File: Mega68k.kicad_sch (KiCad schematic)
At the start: 15 parts, among them J1 CLK Select, J2 Ext CLK, J3 SPI, U1 68000D, U2 AS6C4008-55PCN, U3 AS6C4008-55PCN, X1 CXO_DIP8

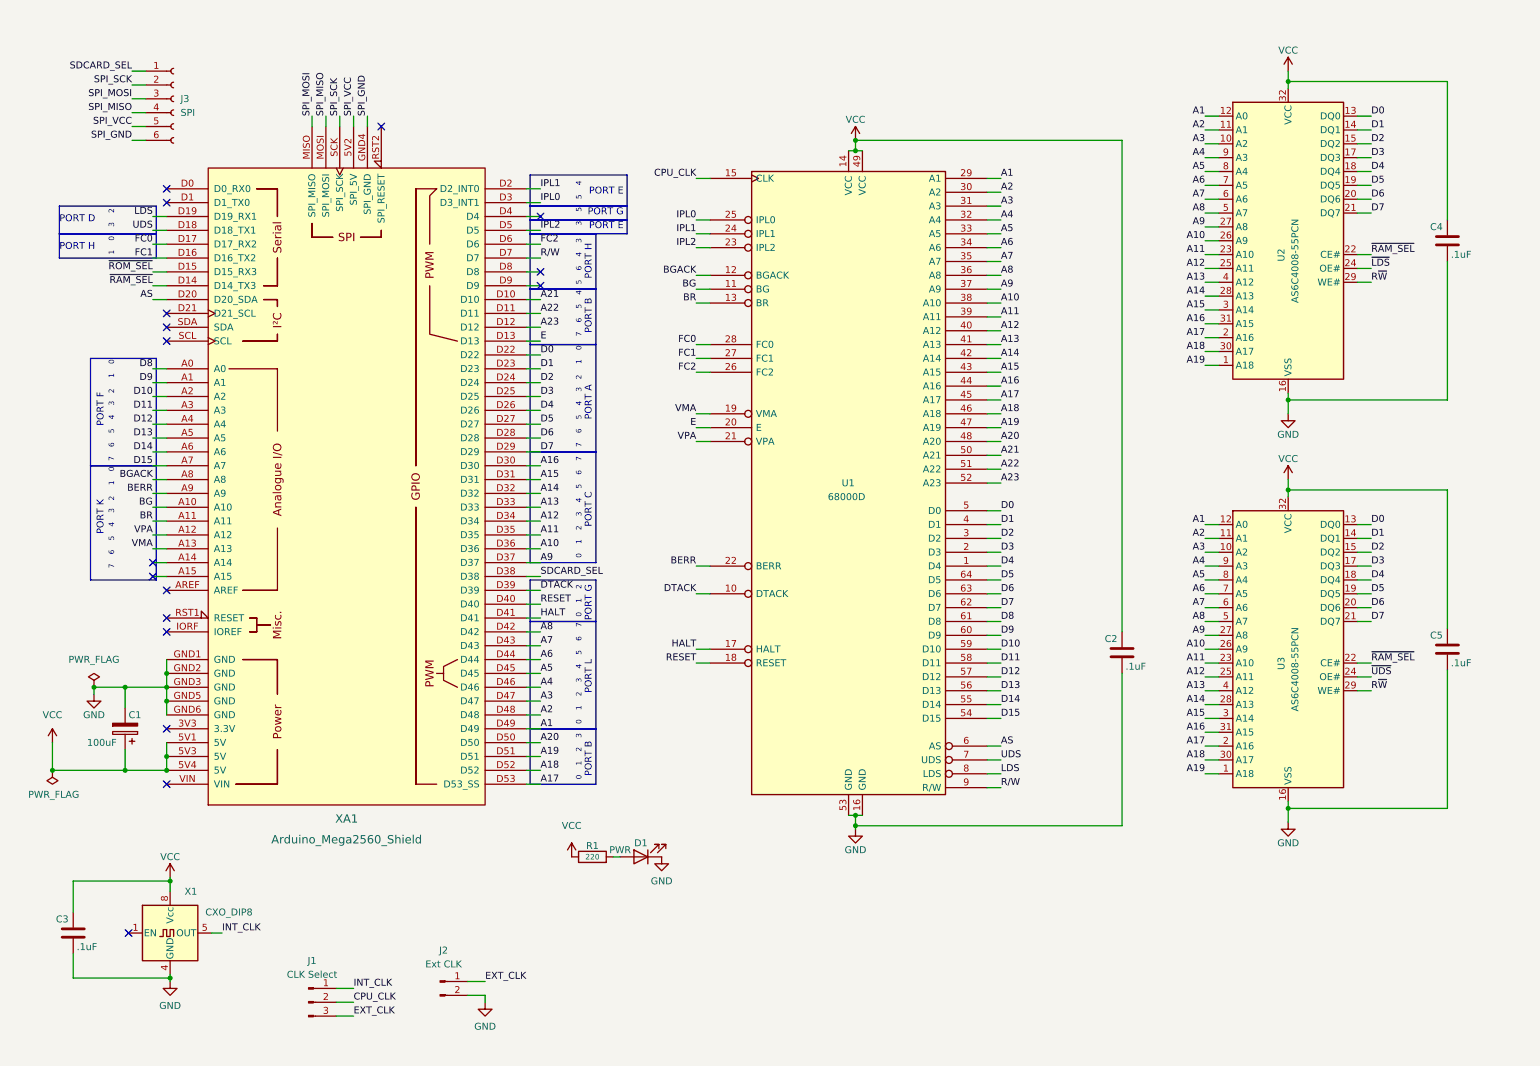
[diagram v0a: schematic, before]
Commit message: Fixed 64 pin socket size and added more status lights
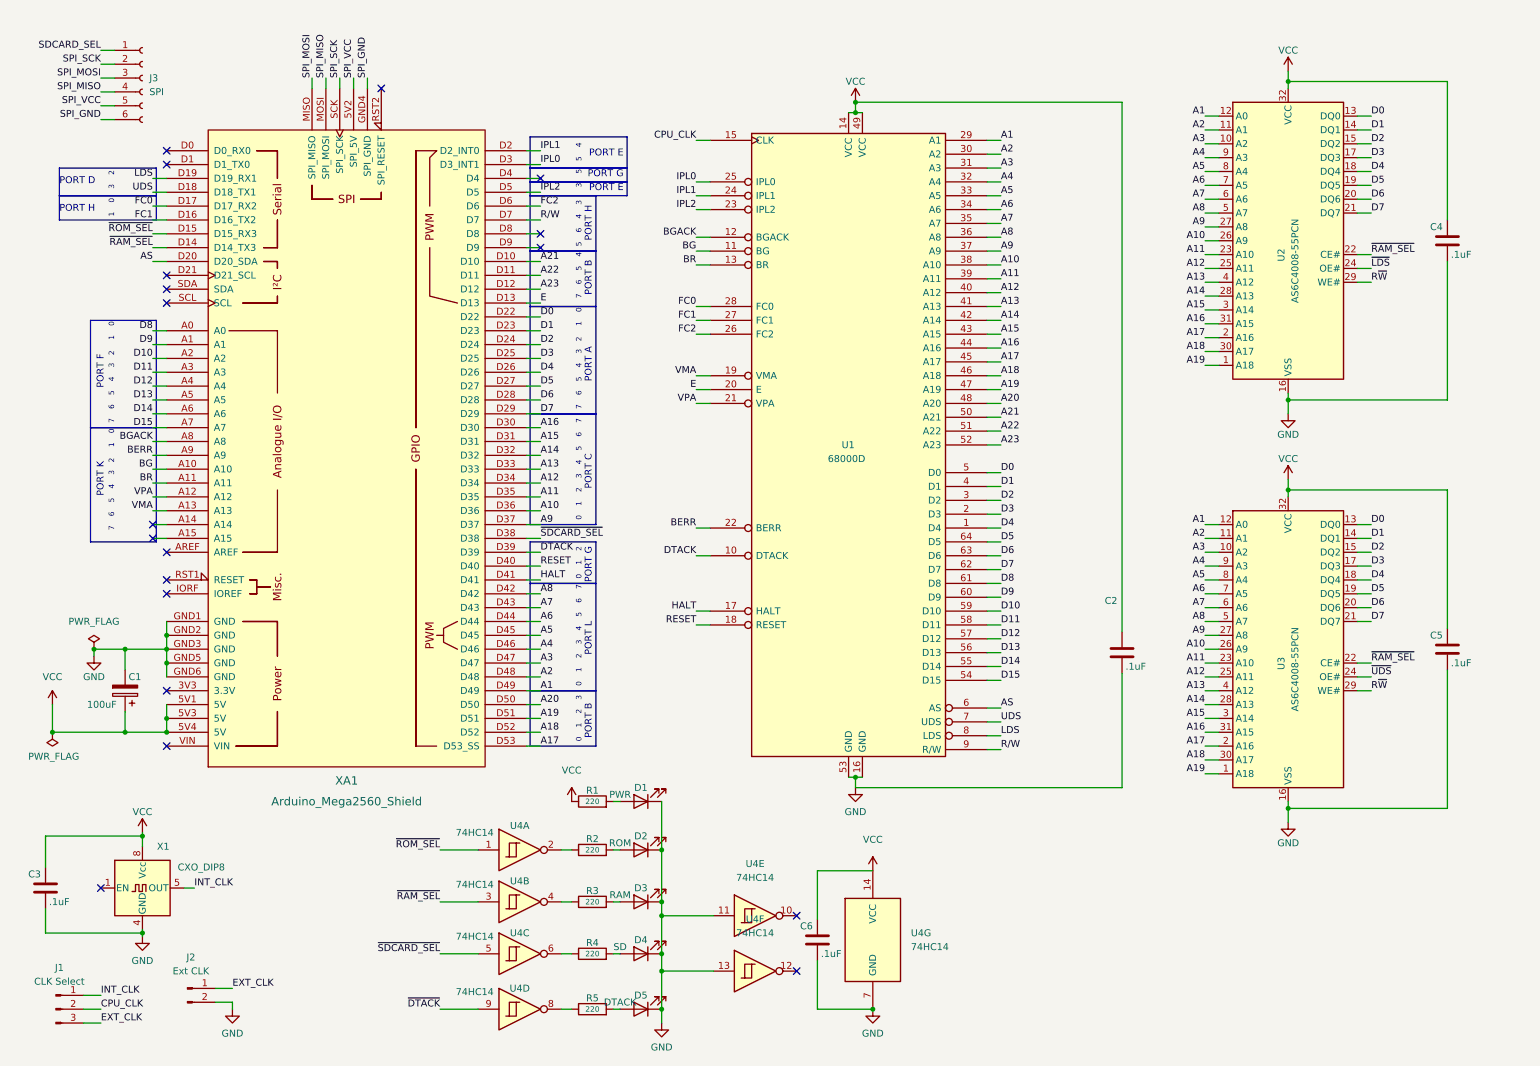
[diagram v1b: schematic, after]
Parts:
- added C6: .1uF, Capacitor_SMD:C_0603_1608Metric, symbol Device:C
- added D2: ROM, LED_SMD:LED_1206_3216Metric, symbol Device:LED
- added D3: RAM, LED_SMD:LED_1206_3216Metric, symbol Device:LED
- added D4: SD, LED_SMD:LED_1206_3216Metric, symbol Device:LED
- added D5: DTACK, LED_SMD:LED_1206_3216Metric, symbol Device:LED
- added R2, R3, R4, R5: 220, Resistor_SMD:R_0603_1608Metric, symbol Device:R
- added U4: 74HC14, Package_SO:SOIC-14_3.9x8.7mm_P1.27mm, symbol 74xx:74HC14
- U1: footprint Package_DIP:DIP-64_W25.4mm_LongPads -> Package_DIP:DIP-64_W22.86mm_Socket
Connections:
- net GND: now also C6.2, D2.1 (K), D3.1 (K), D4.1 (K), D5.1 (K), U4.11, U4.13, U4.7 (GND)
- net SDCARD_SEL: no longer XA1.D38
- net VCC: now also C6.1, U4.14 (VCC)
- net ~{RAM_SEL}: now also U4.3
- net ~{ROM_SEL}: now also U4.1
- new net: D4.2 (A), R4.2
- new net: R4.1, U4.6
- new net: R2.1, U4.2
- new net: D2.2 (A), R2.2
- new net: R3.1, U4.4
- new net: D3.2 (A), R3.2
- new net: D5.2 (A), R5.2
- new net: R5.1, U4.8
- new net ~{DTACK}: U4.9
- new net ~{SDCARD_SEL}: U4.5, XA1.D38
- no-connect marks 17 -> 19
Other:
- moved on the sheet: C1, C3, D1, J1, J2, J3, R1, U1, X1, XA1

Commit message: Added an arduino reset switch
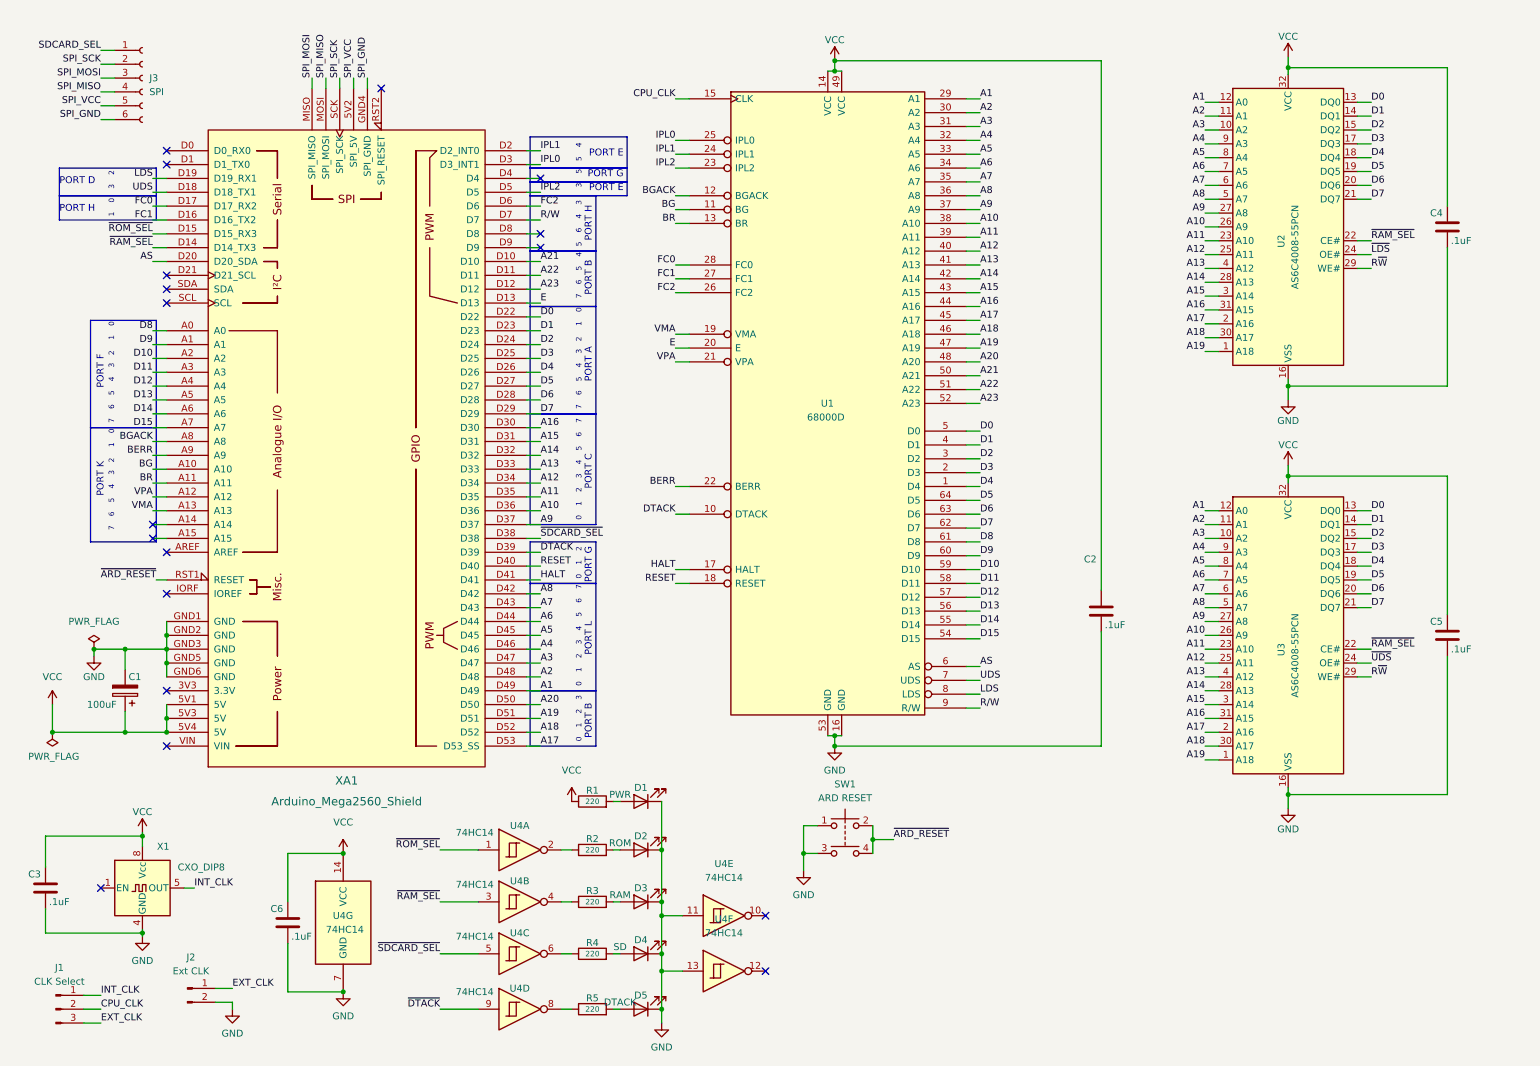
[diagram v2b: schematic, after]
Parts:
- added SW1: ARD RESET, Button_Switch_THT:SW_PUSH_6mm, symbol Switch:SW_Push_Dual
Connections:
- net GND: now also SW1.1, SW1.3
- net ~{ARD_RESET}: now reaches XA1.RST1 (RESET)
- net ~{ARD_RESET}: now also SW1.2, SW1.4
- no-connect marks 19 -> 18
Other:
- moved on the sheet: C2, C4, C5, C6, U1, U2, U3, U4E, U4F, U4G

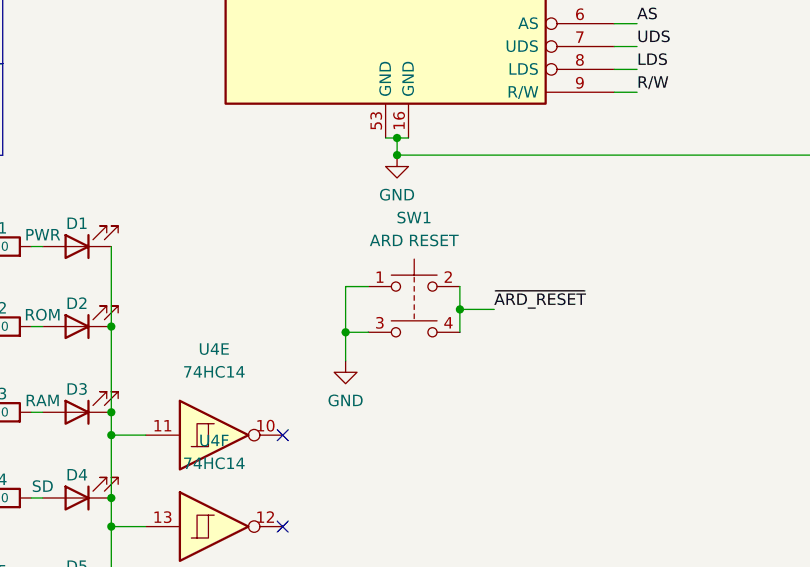
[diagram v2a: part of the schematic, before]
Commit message: Added freerun software sketch for platformio
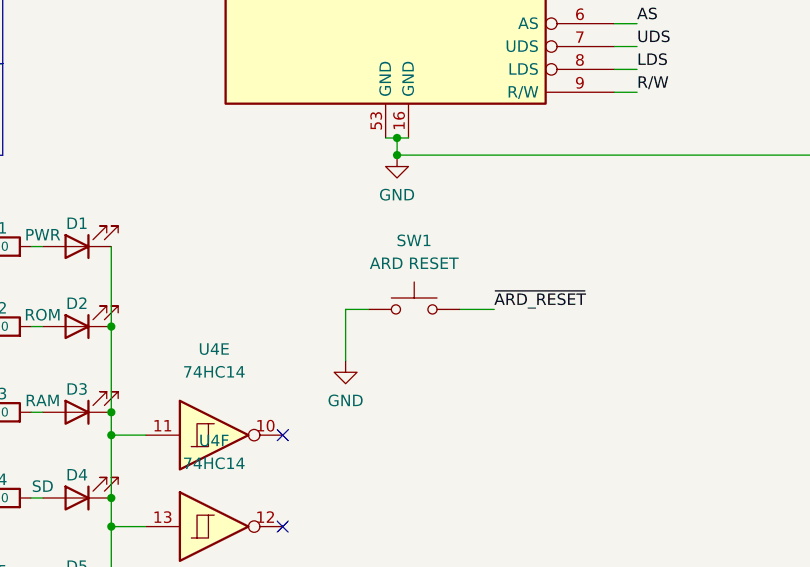
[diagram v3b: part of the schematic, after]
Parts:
- removed SW1: ARD RESET, Button_Switch_THT:SW_PUSH_6mm, symbol Switch:SW_Push_Dual
- added SW1: ARD RESET, symbol Switch:SW_Push
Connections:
- net GND: now also SW1.1
- net ~{ARD_RESET}: now also SW1.2
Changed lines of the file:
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@@
   (junction (at 38.735 141.605) (diameter 0) (color 0 0 0 0)
   )
-  (junction (at 168.275 161.29) (diameter 0) (color 0 0 0 0)
-  )
   (junction (at 244.475 19.685) (diameter 0) (color 0 0 0 0)
   )
@@
   )
   (junction (at 71.12 189.23) (diameter 0) (color 0 0 0 0)
-  )
-  (junction (at 155.575 163.83) (diameter 0) (color 0 0 0 0)
   )
   (junction (at 25.4 126.365) (diameter 0) (color 0 0 0 0)
@@
     (stroke (width 0) (type default) (color 0 0 0 0))
   )
-  (wire (pts (xy 158.115 158.75) (xy 155.575 158.75))
-    (stroke (width 0) (type default) (color 0 0 0 0))
-  )
   (wire (pts (xy 185.42 48.26) (xy 187.96 48.26))
     (stroke (width 0) (type default) (color 0 0 0 0))
@@
     (stroke (width 0) (type default) (color 0 0 0 0))
   )
-  (wire (pts (xy 168.275 158.75) (xy 168.275 161.29))
-    (stroke (width 0) (type default) (color 0 0 0 0))
-  )
   (wire (pts (xy 132.08 68.58) (xy 134.62 68.58))
     (stroke (width 0) (type default) (color 0 0 0 0))
@@
     (stroke (width 0) (type default) (color 0 0 0 0))
   )
-  (wire (pts (xy 168.275 161.29) (xy 168.275 163.83))
-    (stroke (width 0) (type default) (color 0 0 0 0))
-  )
   (wire (pts (xy 257.175 126.365) (xy 259.715 126.365))
     (stroke (width 0) (type default) (color 0 0 0 0))
@@
     (stroke (width 0) (type default) (color 0 0 0 0))
   )
+  (wire (pts (xy 155.575 161.29) (xy 158.115 161.29))
+    (stroke (width 0) (type default) (color 0 0 0 0))
+  )
   (wire (pts (xy 257.175 106.045) (xy 259.715 106.045))
     (stroke (width 0) (type default) (color 0 0 0 0))
@@
     (stroke (width 0) (type default) (color 0 0 0 0))
   )
-  (wire (pts (xy 155.575 163.83) (xy 155.575 167.005))
-    (stroke (width 0) (type default) (color 0 0 0 0))
-  )
   (wire (pts (xy 104.775 57.785) (xy 107.315 57.785))
     (stroke (width 0) (type default) (color 0 0 0 0))
@@
     (stroke (width 0) (type default) (color 0 0 0 0))
   )
-  (wire (pts (xy 155.575 163.83) (xy 158.115 163.83))
-    (stroke (width 0) (type default) (color 0 0 0 0))
-  )
   (wire (pts (xy 88.9 163.195) (xy 95.885 163.195))
     (stroke (width 0) (type default) (color 0 0 0 0))
   )
+  (wire (pts (xy 155.575 161.29) (xy 155.575 167.005))
+    (stroke (width 0) (type default) (color 0 0 0 0))
+  )
   (wire (pts (xy 229.235 118.745) (xy 231.775 118.745))
     (stroke (width 0) (type default) (color 0 0 0 0))
@@
   )
   (wire (pts (xy 257.175 131.445) (xy 259.715 131.445))
-    (stroke (width 0) (type default) (color 0 0 0 0))
-  )
-  (wire (pts (xy 155.575 158.75) (xy 155.575 163.83))
     (stroke (width 0) (type default) (color 0 0 0 0))
   )
@@
     (pin "4")
   )
+  (symbol (lib_id "Switch:SW_Push") (at 163.195 161.29 0) (unit 1)
+    (in_bom yes) (on_board yes) (fields_autoplaced)
+    (property "Reference" "SW1" (id 0) (at 163.195 153.67 0))
+    (property "Value" "ARD RESET" (id 1) (at 163.195 156.21 0))
+    (property "Footprint" "" (id 2) (at 163.195 156.21 0)
+      (effects (font (size 1.27 1.27)) hide)
+    )
+    (property "Datasheet" "~" (id 3) (at 163.195 156.21 0)
+      (effects (font (size 1.27 1.27)) hide)
+    )
+    (pin "1")
+    (pin "2")
+  )
   (symbol (lib_id "Connector:Conn_01x03_Male") (at 18.415 192.405 0) (unit 1)
     (in_bom yes) (on_board yes) (fields_autoplaced)
@@
     )
     (pin "1")
-  )
-  (symbol (lib_id "Switch:SW_Push_Dual") (at 163.195 158.75 0) (unit 1)
-    (in_bom yes) (on_board yes) (fields_autoplaced)
-    (property "Reference" "SW1" (id 0) (at 163.195 151.13 0))
-    (property "Value" "ARD RESET" (id 1) (at 163.195 153.67 0))
-    (property "Footprint" "Button_Switch_THT:SW_PUSH_6mm" (id 2) (at 163.195 153.67 0)
-      (effects (font (size 1.27 1.27)) hide)
-    )
-    (property "Datasheet" "~" (id 3) (at 163.195 153.67 0)
-      (effects (font (size 1.27 1.27)) hide)
-    )
-    (pin "1")
-    (pin "2")
-    (pin "3")
-    (pin "4")
   )
   (symbol (lib_id "Oscillator:CXO_DIP8") (at 34.29 170.18 0) (unit 1)
@@
       (reference "R5") (unit 1) (value "220") (footprint "Resistor_SMD:R_0603_1608Metric")
     )
-    (path "/ead914e2-e9fa-4ef4-91e8-61168d6a1cba"
-      (reference "SW1") (unit 1) (value "ARD RESET") (footprint "Button_Switch_THT:SW_PUSH_6mm")
+    (path "/aa79ed5f-e950-41a8-a4a3-e9e667ea0c78"
+      (reference "SW1") (unit 1) (value "ARD RESET") (footprint "")
     )
     (path "/71b28aa2-5872-4b2d-ac35-9163f8849193"

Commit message: Working freerun
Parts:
- removed C4, C5, C6: .1uF, Capacitor_SMD:C_0603_1608Metric, symbol Device:C
- removed D2: ROM, LED_SMD:LED_1206_3216Metric, symbol Device:LED
- removed D3: RAM, LED_SMD:LED_1206_3216Metric, symbol Device:LED
- removed D4: SD, LED_SMD:LED_1206_3216Metric, symbol Device:LED
- removed D5: DTACK, LED_SMD:LED_1206_3216Metric, symbol Device:LED
- removed R2, R3, R4, R5: 220, Resistor_SMD:R_0603_1608Metric, symbol Device:R
- removed U2, U3: AS6C4008-55PCN, Package_SO:SSOP-32_11.305x20.495mm_P1.27mm, symbol Memory_RAM:AS6C4008-55PCN
- removed U4: 74HC14, Package_SO:SOIC-14_3.9x8.7mm_P1.27mm, symbol 74xx:74HC14
- added C7: .1uF, Capacitor_SMD:C_0603_1608Metric, symbol Device:C
- added J4: Debug, Connector_PinHeader_2.54mm:PinHeader_2x34_P2.54mm_Vertical, symbol Connector_Generic:Conn_02x34_Odd_Even
- added R6: 10k, Resistor_SMD:R_0603_1608Metric, symbol Device:R
- added SW2: CPU_RESET, Button_Switch_THT:SW_PUSH_6mm, symbol Switch:SW_Push
- SW1: footprint (none) -> Button_Switch_THT:SW_PUSH_6mm
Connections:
- net A1: now also J4.3 (Pin_3)
- net A10: now also J4.12 (Pin_12)
- net A11: now also J4.13 (Pin_13)
- net A12: now also J4.14 (Pin_14)
- net A13: now also J4.15 (Pin_15)
- net A14: now also J4.16 (Pin_16)
- net A15: now also J4.17 (Pin_17)
- net A16: now also J4.18 (Pin_18)
- net A17: now also J4.19 (Pin_19)
- net A18: now also J4.20 (Pin_20)
- net A19: now also J4.21 (Pin_21)
- net A2: now also J4.4 (Pin_4)
- net A20: now also J4.22 (Pin_22)
- net A21: now also J4.23 (Pin_23)
- net A22: now also J4.24 (Pin_24)
- net A23: now also J4.25 (Pin_25)
- net A3: now also J4.5 (Pin_5)
- net A4: now also J4.6 (Pin_6)
- net A5: now also J4.7 (Pin_7)
- net A6: now also J4.8 (Pin_8)
- net A7: now also J4.9 (Pin_9)
- net A8: now also J4.10 (Pin_10)
- net A9: now also J4.11 (Pin_11)
- net BERR: now also J4.49 (Pin_49)
- net BG: now also J4.56 (Pin_56)
- net BGACK: now also J4.53 (Pin_53)
- net BR: now also J4.55 (Pin_55)
- net CPU_CLK: now also J4.42 (Pin_42)
- net D0: now also J4.26 (Pin_26)
- net D1: now also J4.27 (Pin_27)
- net D10: now also J4.36 (Pin_36)
- net D11: now also J4.37 (Pin_37)
- net D12: now also J4.38 (Pin_38)
- net D13: now also J4.39 (Pin_39)
- net D14: now also J4.40 (Pin_40)
- net D15: now also J4.41 (Pin_41)
- net D2: now also J4.28 (Pin_28)
- net D3: now also J4.29 (Pin_29)
- net D4: now also J4.30 (Pin_30)
- net D5: now also J4.31 (Pin_31)
- net D6: now also J4.32 (Pin_32)
- net D7: now also J4.33 (Pin_33)
- net D8: now also J4.34 (Pin_34)
- net D9: now also J4.35 (Pin_35)
- net DTACK: now also J4.50 (Pin_50)
- net E: now also J4.51 (Pin_51)
- net FC0: now also J4.60 (Pin_60)
- net FC1: now also J4.61 (Pin_61)
- net FC2: now also J4.62 (Pin_62)
- net GND: now also C7.2, J4.1 (Pin_1), J4.2 (Pin_2), R6.2
- net HALT: now also J4.48 (Pin_48)
- net INT_CLK: now also XA1.D21 (D21_SCL)
- net IPL0: now also J4.57 (Pin_57)
- net IPL1: now also J4.58 (Pin_58)
- net IPL2: now also J4.59 (Pin_59)
- net RESET: now also J4.47 (Pin_47)
- net R~{W}: now also J4.43 (Pin_43)
- net VCC: now also C7.1, J4.67 (Pin_67), J4.68 (Pin_68), SW2.2
- net VMA: now also J4.52 (Pin_52)
- net VPA: now also J4.54 (Pin_54)
- net ~{LDS}: now also J4.46 (Pin_46)
- net ~{RAM_SEL}: now also J4.64 (Pin_64)
- net ~{ROM_SEL}: now also J4.63 (Pin_63)
- net ~{SDCARD_SEL}: now also J4.65 (Pin_65)
- net ~{UDS}: now also J4.45 (Pin_45)
- net CPU_RST: now reaches XA1.D4
- net CPU_RST: now also R6.1, SW2.1
- new net ~{AS}: J4.44 (Pin_44)
- no-connect marks 18 -> 15
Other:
- moved on the sheet: C2, C3, D1, J1, J2, R1, SW1, U1, X1
